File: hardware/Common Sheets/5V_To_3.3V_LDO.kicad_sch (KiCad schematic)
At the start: 3 parts, among them U2 TLV71333PDBV

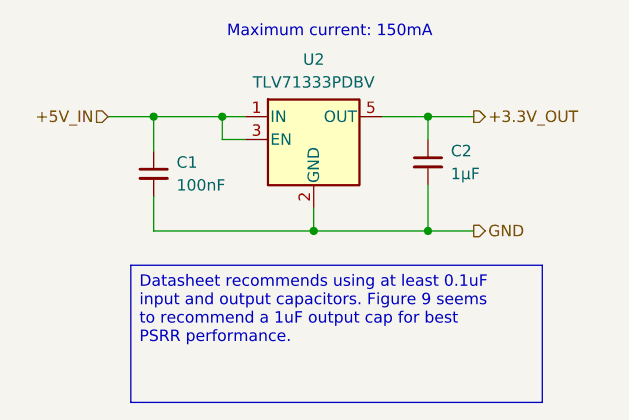
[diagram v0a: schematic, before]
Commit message: Implement card connector schematic
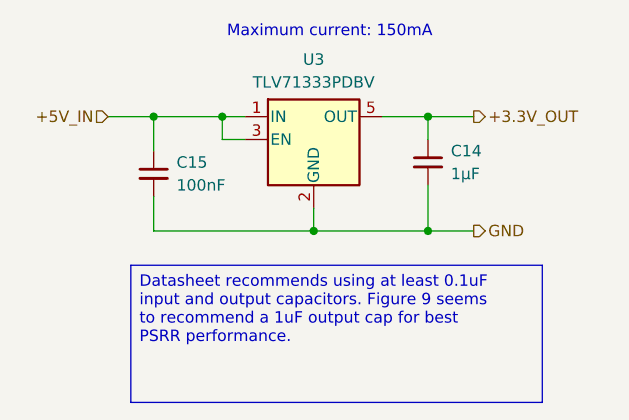
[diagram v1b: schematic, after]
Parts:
- C14: renamed from C2; LibRef CL10B105MO8NNWC -> (none)
- C15: renamed from C1; LibRef ESD35C104K4T2A-24 -> (none)
- renumbered U2 to U3
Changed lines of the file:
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@@
 		(dnp no)
 		(fields_autoplaced yes)
-		(property "Reference" "U2"
+		(property "Reference" "U3"
 			(at 74.93 44.45 0)
 			(effects
@@
 		)
 		(instances
-			(project "Main Unit"
-				(path "/7d91f165-331a-4c48-9d02-ee2a0aa7e94a/3aa6cc73-4b82-4451-98a6-fa9c80108c23"
-					(reference "U2")
+			(project "HackerDAQ Voltage Card"
+				(path "/af2d881c-6553-449d-9093-6deb41497bdc/8683fa8f-1b23-40d2-8dab-5a640e39446f"
+					(reference "U3")
 					(unit 1)
 				)
@@
 		(dnp no)
 		(fields_autoplaced yes)
-		(property "Reference" "C2"
+		(property "Reference" "C14"
 			(at 90.17 54.6162 0)
 			(effects
@@
 			)
 		)
-		(property "LibRef" "CL10B105MO8NNWC"
-			(at 87.63 55.88 0)
-			(effects
-				(font
-					(size 1.27 1.27)
-				)
-				(hide yes)
-			)
-		)
 		(pin "1"
 		)
@@
 		)
 		(instances
-			(project "Main Unit"
-				(path "/7d91f165-331a-4c48-9d02-ee2a0aa7e94a/3aa6cc73-4b82-4451-98a6-fa9c80108c23"
-					(reference "C2")
+			(project "HackerDAQ Voltage Card"
+				(path "/af2d881c-6553-449d-9093-6deb41497bdc/8683fa8f-1b23-40d2-8dab-5a640e39446f"
+					(reference "C14")
 					(unit 1)
 				)
@@
 		(dnp no)
 		(fields_autoplaced yes)
-		(property "Reference" "C1"
+		(property "Reference" "C15"
 			(at 59.69 55.8862 0)
 			(effects
@@
 			)
 		)
-		(property "LibRef" "ESD35C104K4T2A-24"
-			(at 57.15 57.15 0)
-			(effects
-				(font
-					(size 1.27 1.27)
-				)
-				(hide yes)
-			)
-		)
 		(pin "1"
 		)
@@
 		)
 		(instances
-			(project "Main Unit"
-				(path "/7d91f165-331a-4c48-9d02-ee2a0aa7e94a/3aa6cc73-4b82-4451-98a6-fa9c80108c23"
-					(reference "C1")
+			(project "HackerDAQ Voltage Card"
+				(path "/af2d881c-6553-449d-9093-6deb41497bdc/8683fa8f-1b23-40d2-8dab-5a640e39446f"
+					(reference "C15")
 					(unit 1)
 				)

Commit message: Start on MCU symbol and main unit
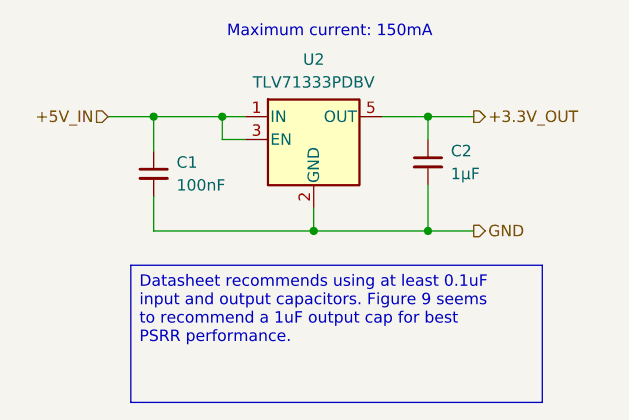
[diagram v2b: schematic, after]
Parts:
- C1: renamed from C15; LibRef (none) -> ESD35C104K4T2A-24
- C2: renamed from C14; LibRef (none) -> CL10B105MO8NNWC
- renumbered U3 to U2
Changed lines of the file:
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@@
 		(dnp no)
 		(fields_autoplaced yes)
-		(property "Reference" "U3"
+		(property "Reference" "U2"
 			(at 74.93 44.45 0)
 			(effects
@@
 		)
 		(instances
-			(project "HackerDAQ Voltage Card"
-				(path "/af2d881c-6553-449d-9093-6deb41497bdc/8683fa8f-1b23-40d2-8dab-5a640e39446f"
-					(reference "U3")
+			(project "Main Unit"
+				(path "/7d91f165-331a-4c48-9d02-ee2a0aa7e94a/3aa6cc73-4b82-4451-98a6-fa9c80108c23"
+					(reference "U2")
 					(unit 1)
 				)
@@
 		(dnp no)
 		(fields_autoplaced yes)
-		(property "Reference" "C14"
+		(property "Reference" "C2"
 			(at 90.17 54.6162 0)
 			(effects
@@
 			)
 		)
+		(property "LibRef" "CL10B105MO8NNWC"
+			(at 87.63 55.88 0)
+			(effects
+				(font
+					(size 1.27 1.27)
+				)
+				(hide yes)
+			)
+		)
 		(pin "1"
 		)
@@
 		)
 		(instances
-			(project "HackerDAQ Voltage Card"
-				(path "/af2d881c-6553-449d-9093-6deb41497bdc/8683fa8f-1b23-40d2-8dab-5a640e39446f"
-					(reference "C14")
+			(project "Main Unit"
+				(path "/7d91f165-331a-4c48-9d02-ee2a0aa7e94a/3aa6cc73-4b82-4451-98a6-fa9c80108c23"
+					(reference "C2")
 					(unit 1)
 				)
@@
 		(dnp no)
 		(fields_autoplaced yes)
-		(property "Reference" "C15"
+		(property "Reference" "C1"
 			(at 59.69 55.8862 0)
 			(effects
@@
 			)
 		)
+		(property "LibRef" "ESD35C104K4T2A-24"
+			(at 57.15 57.15 0)
+			(effects
+				(font
+					(size 1.27 1.27)
+				)
+				(hide yes)
+			)
+		)
 		(pin "1"
 		)
@@
 		)
 		(instances
-			(project "HackerDAQ Voltage Card"
-				(path "/af2d881c-6553-449d-9093-6deb41497bdc/8683fa8f-1b23-40d2-8dab-5a640e39446f"
-					(reference "C15")
+			(project "Main Unit"
+				(path "/7d91f165-331a-4c48-9d02-ee2a0aa7e94a/3aa6cc73-4b82-4451-98a6-fa9c80108c23"
+					(reference "C1")
 					(unit 1)
 				)
